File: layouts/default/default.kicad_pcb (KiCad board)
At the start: 2 copper layers, 120 x 130 mm, 87 parts

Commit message: how could i forget the silkscreen art??
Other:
- board text added: "your cellz here xD"

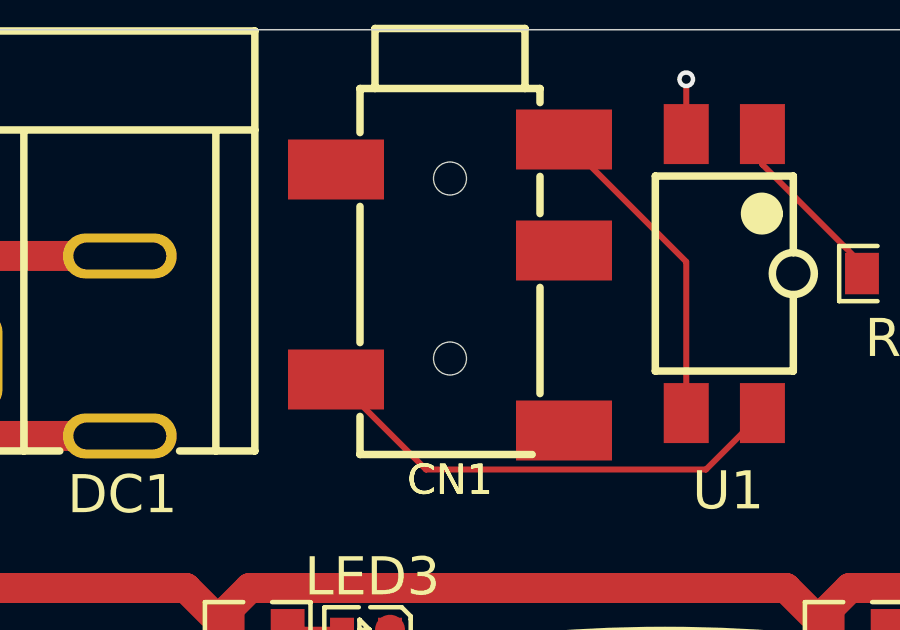
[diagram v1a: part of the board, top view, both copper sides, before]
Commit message: add the T ~ R trace, redo the fill zone and rebuild the gerbers
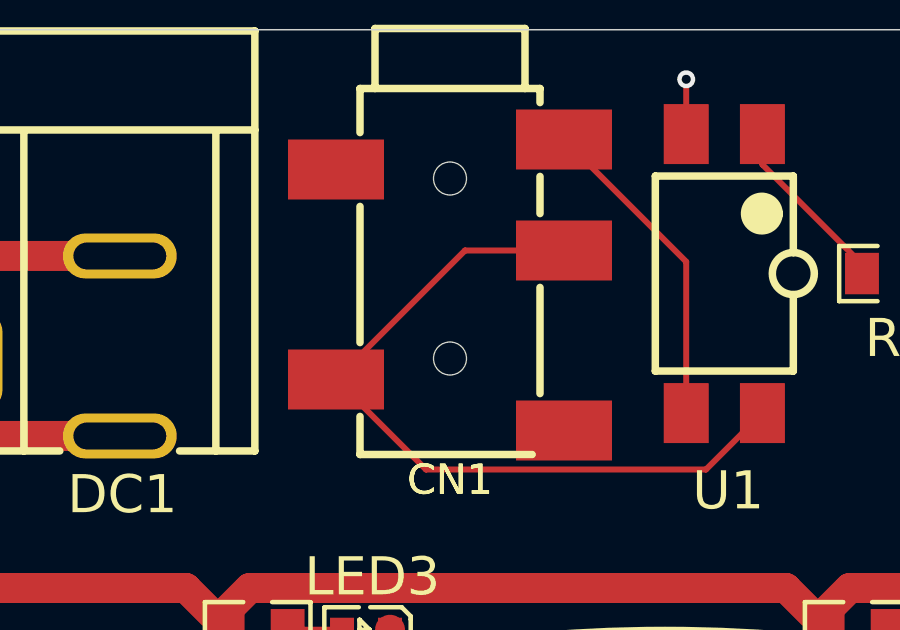
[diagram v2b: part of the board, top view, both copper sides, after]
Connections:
- net footprint-T-1 renamed T
- CN1 pad 3: footprint-R-1 -> footprint-R-0
- CN1 pad 4: footprint-T-0 -> footprint-R-0
- CN2 pad 3: footprint-R-0 -> footprint-R-1
- R2 pad 1: footprint-R-0 -> footprint-R-1
- U1 pad 4: footprint-T-0 -> footprint-R-0
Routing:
- net footprint-R-0: track 3.08 -> 25.6 mm
- net footprint-T-0: track 16.2 -> 0.00 mm
- net footprint-R-1: track 0.00 -> 3.08 mm
